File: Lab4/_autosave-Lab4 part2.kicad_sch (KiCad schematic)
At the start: 10 parts, among them J1 Conn_01x02_Male, U1 NE555D

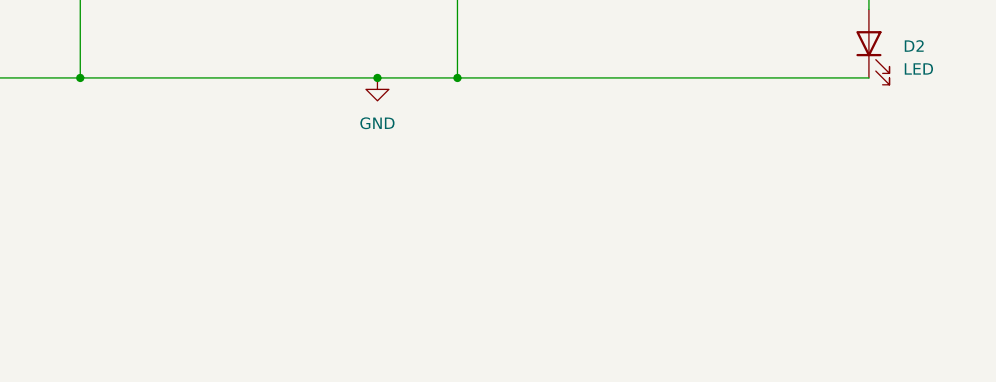
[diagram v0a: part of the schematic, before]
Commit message: Y direction and 2 netlabels update
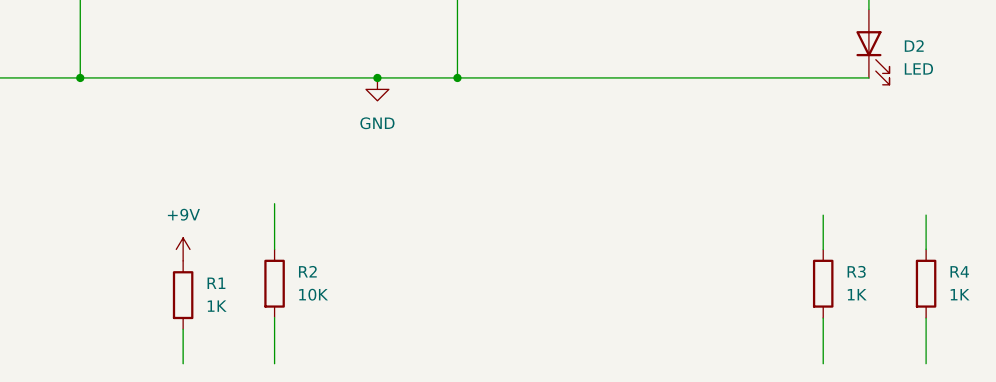
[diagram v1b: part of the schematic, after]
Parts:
- added R1, R3, R4: 1K, symbol Device:R
- added R2: 10K, symbol Device:R
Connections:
- net +9V: now also R1.1
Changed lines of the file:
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@@
+    (stroke (width 0) (type default) (color 0 0 0 0))
+  )
+  (wire (pts (xy 110.49 138.43) (xy 110.49 143.51))
+    (stroke (width 0) (type default) (color 0 0 0 0))
+  )
+  (wire (pts (xy 171.45 127) (xy 171.45 130.81))
     (stroke (width 0) (type default) (color 0 0 0 0))
   )
@@
     (stroke (width 0) (type default) (color 0 0 0 0))
   )
+  (wire (pts (xy 171.45 138.43) (xy 171.45 143.51))
+    (stroke (width 0) (type default) (color 0 0 0 0))
+  )
   (wire (pts (xy 69.85 87.63) (xy 69.85 97.79))
     (stroke (width 0) (type default) (color 0 0 0 0))
@@
     (stroke (width 0) (type default) (color 0 0 0 0))
   )
+  (wire (pts (xy 100.33 139.7) (xy 100.33 143.51))
+    (stroke (width 0) (type default) (color 0 0 0 0))
+  )
   (wire (pts (xy 60.96 68.58) (xy 69.85 68.58))
     (stroke (width 0) (type default) (color 0 0 0 0))
@@
     (stroke (width 0) (type default) (color 0 0 0 0))
   )
+  (wire (pts (xy 182.88 138.43) (xy 182.88 143.51))
+    (stroke (width 0) (type default) (color 0 0 0 0))
+  )
   (wire (pts (xy 110.49 81.28) (xy 118.11 81.28))
     (stroke (width 0) (type default) (color 0 0 0 0))
   )
+  (wire (pts (xy 182.88 127) (xy 182.88 130.81))
+    (stroke (width 0) (type default) (color 0 0 0 0))
+  )
   (wire (pts (xy 88.9 111.76) (xy 121.92 111.76))
     (stroke (width 0) (type default) (color 0 0 0 0))
@@
   )
   (wire (pts (xy 60.96 97.79) (xy 69.85 97.79))
+    (stroke (width 0) (type default) (color 0 0 0 0))
+  )
+  (wire (pts (xy 110.49 125.73) (xy 110.49 130.81))
     (stroke (width 0) (type default) (color 0 0 0 0))
   )
@@
     (effects (font (size 1.27 1.27)) (justify left bottom))
   )
+  (symbol (lib_id "Device:R") (at 171.45 134.62 0) (unit 1)
+    (in_bom yes) (on_board yes)
+    (property "Reference" "R3" (id 0) (at 173.99 133.3499 0)
+      (effects (font (size 1.27 1.27)) (justify left))
+    )
+    (property "Value" "1K" (id 1) (at 173.99 135.8899 0)
+      (effects (font (size 1.27 1.27)) (justify left))
+    )
+    (property "Footprint" "" (id 2) (at 169.672 134.62 90)
+      (effects (font (size 1.27 1.27)) hide)
+    )
+    (property "Datasheet" "~" (id 3) (at 171.45 134.62 0)
+      (effects (font (size 1.27 1.27)) hide)
+    )
+    (pin "1")
+    (pin "2")
+  )
   (symbol (lib_id "power:+9V") (at 124.46 25.4 0) (unit 1)
     (in_bom yes) (on_board yes) (fields_autoplaced)
-    (property "Reference" "#PWR?" (id 0) (at 124.46 29.21 0)
+    (property "Reference" "#PWR01" (id 0) (at 124.46 29.21 0)
       (effects (font (size 1.27 1.27)) hide)
     )
@@
     (pin "2")
   )
+  (symbol (lib_id "Device:R") (at 100.33 135.89 0) (unit 1)
+    (in_bom yes) (on_board yes) (fields_autoplaced)
+    (property "Reference" "R1" (id 0) (at 102.87 134.6199 0)
+      (effects (font (size 1.27 1.27)) (justify left))
+    )
+    (property "Value" "1K" (id 1) (at 102.87 137.1599 0)
+      (effects (font (size 1.27 1.27)) (justify left))
+    )
+    (property "Footprint" "" (id 2) (at 98.552 135.89 90)
+      (effects (font (size 1.27 1.27)) hide)
+    )
+    (property "Datasheet" "~" (id 3) (at 100.33 135.89 0)
+      (effects (font (size 1.27 1.27)) hide)
+    )
+    (pin "1")
+    (pin "2")
+  )
   (symbol (lib_id "Device:LED") (at 176.53 107.95 90) (unit 1)
     (in_bom yes) (on_board yes) (fields_autoplaced)
@@
   (symbol (lib_id "power:GND") (at 127 25.4 180) (unit 1)
     (in_bom yes) (on_board yes)
-    (property "Reference" "#PWR?" (id 0) (at 127 19.05 0)
+    (property "Reference" "#PWR02" (id 0) (at 127 19.05 0)
       (effects (font (size 1.27 1.27)) hide)
     )
@@
   (symbol (lib_id "power:+9V") (at 69.85 50.8 0) (unit 1)
     (in_bom yes) (on_board yes) (fields_autoplaced)
-    (property "Reference" "#PWR?" (id 0) (at 69.85 54.61 0)
+    (property "Reference" "#PWR04" (id 0) (at 69.85 54.61 0)
       (effects (font (size 1.27 1.27)) hide)
     )
@@
     (pin "2")
   )
+  (symbol (lib_id "Device:R") (at 182.88 134.62 0) (unit 1)
+    (in_bom yes) (on_board yes)
+    (property "Reference" "R4" (id 0) (at 185.42 133.3499 0)
+      (effects (font (size 1.27 1.27)) (justify left))
+    )
+    (property "Value" "1K" (id 1) (at 185.42 135.8899 0)
+      (effects (font (size 1.27 1.27)) (justify left))
+    )
+    (property "Footprint" "" (id 2) (at 181.102 134.62 90)
+      (effects (font (size 1.27 1.27)) hide)
+    )
+    (property "Datasheet" "~" (id 3) (at 182.88 134.62 0)
+      (effects (font (size 1.27 1.27)) hide)
+    )
+    (pin "1")
+    (pin "2")
+  )
   (symbol (lib_id "Device:R") (at 69.85 54.61 0) (unit 1)
     (in_bom yes) (on_board yes) (fields_autoplaced)
@@
   (symbol (lib_id "power:+9V") (at 176.53 44.45 0) (unit 1)
     (in_bom yes) (on_board yes) (fields_autoplaced)
-    (property "Reference" "#PWR?" (id 0) (at 176.53 48.26 0)
+    (property "Reference" "#PWR03" (id 0) (at 176.53 48.26 0)
       (effects (font (size 1.27 1.27)) hide)
     )
@@
     (pin "1")
   )
+  (symbol (lib_id "power:+9V") (at 100.33 132.08 0) (unit 1)
+    (in_bom yes) (on_board yes) (fields_autoplaced)
+    (property "Reference" "#PWR07" (id 0) (at 100.33 135.89 0)
+      (effects (font (size 1.27 1.27)) hide)
+    )
+    (property "Value" "+9V" (id 1) (at 100.33 127 0))
+    (property "Footprint" "" (id 2) (at 100.33 132.08 0)
+      (effects (font (size 1.27 1.27)) hide)
+    )
+    (property "Datasheet" "" (id 3) (at 100.33 132.08 0)
+      (effects (font (size 1.27 1.27)) hide)
+    )
+    (pin "1")
+  )
   (symbol (lib_id "power:GND") (at 121.92 111.76 0) (unit 1)
     (in_bom yes) (on_board yes) (fields_autoplaced)
-    (property "Reference" "#PWR?" (id 0) (at 121.92 118.11 0)
+    (property "Reference" "#PWR06" (id 0) (at 121.92 118.11 0)
       (effects (font (size 1.27 1.27)) hide)
     )
@@
   (symbol (lib_id "power:+9V") (at 130.81 58.42 0) (unit 1)
     (in_bom yes) (on_board yes) (fields_autoplaced)
-    (property "Reference" "#PWR?" (id 0) (at 130.81 62.23 0)
+    (property "Reference" "#PWR05" (id 0) (at 130.81 62.23 0)
       (effects (font (size 1.27 1.27)) hide)
     )
@@
     )
     (pin "1")
+  )
+  (symbol (lib_id "Device:R") (at 110.49 134.62 0) (unit 1)
+    (in_bom yes) (on_board yes) (fields_autoplaced)
+    (property "Reference" "R2" (id 0) (at 113.03 133.3499 0)
+      (effects (font (size 1.27 1.27)) (justify left))
+    )
+    (property "Value" "10K" (id 1) (at 113.03 135.8899 0)
+      (effects (font (size 1.27 1.27)) (justify left))
+    )
+    (property "Footprint" "" (id 2) (at 108.712 134.62 90)
+      (effects (font (size 1.27 1.27)) hide)
+    )
+    (property "Datasheet" "~" (id 3) (at 110.49 134.62 0)
+      (effects (font (size 1.27 1.27)) hide)
+    )
+    (pin "1")
+    (pin "2")
   )
   (symbol (lib_id "Device:R") (at 176.53 66.04 0) (unit 1)
@@
   (symbol_instances
     (path "/282a963d-bfb8-4d94-9bf6-62b851b06003"
-      (reference "#PWR?") (unit 1) (value "+9V") (footprint "")
+      (reference "#PWR01") (unit 1) (value "+9V") (footprint "")
     )
     (path "/5d09f4c4-a044-47ca-ac71-306d51ef7f90"
-      (reference "#PWR?") (unit 1) (value "GND") (footprint "")
+      (reference "#PWR02") (unit 1) (value "GND") (footprint "")
+    )
+    (path "/b412588f-978c-4331-ae0a-8423d483384c"
+      (reference "#PWR03") (unit 1) (value "+9V") (footprint "")
     )
     (path "/74069aab-7706-4166-a931-cdf4c5448779"
-      (reference "#PWR?") (unit 1) (value "+9V") (footprint "")
-    )
-    (path "/b412588f-978c-4331-ae0a-8423d483384c"
-      (reference "#PWR?") (unit 1) (value "+9V") (footprint "")
+      (reference "#PWR04") (unit 1) (value "+9V") (footprint "")
+    )
+    (path "/c17c992d-526c-4279-bbbc-3fdfc491b0ff"
+      (reference "#PWR05") (unit 1) (value "+9V") (footprint "")
     )
     (path "/bcee0015-7b8e-4b42-a656-2b391cf11282"
-      (reference "#PWR?") (unit 1) (value "GND") (footprint "")
-    )
-    (path "/c17c992d-526c-4279-bbbc-3fdfc491b0ff"
-      (reference "#PWR?") (unit 1) (value "+9V") (footprint "")
+      (reference "#PWR06") (unit 1) (value "GND") (footprint "")
+    )
+    (path "/b8ebe7e4-57a8-4fda-9b97-02cec9d370ef"
+      (reference "#PWR07") (unit 1) (value "+9V") (footprint "")
     )
     (path "/c045f09e-98f2-4d47-a454-cfd2caa9b0cd"
@@
       (reference "J1") (unit 1) (value "Conn_01x02_Male") (footprint "")
     )
+    (path "/4cc59900-8c63-40da-899a-0fa5b085c4e7"
+      (reference "R1") (unit 1) (value "1K") (footprint "")
+    )
     (path "/b3516c82-4832-4970-a96f-5101ef3a446b"
       (reference "R1") (unit 1) (value "1K") (footprint "")
     )
+    (path "/cf21566b-861a-4450-a59b-8a46c6eb49e6"
+      (reference "R2") (unit 1) (value "10K") (footprint "")
+    )
     (path "/f7a918f5-f477-4015-8f3d-6de4b24bd234"
       (reference "R2") (unit 1) (value "10K") (footprint "")
     )
+    (path "/26e5687a-a9a4-4ea7-a907-b7227bd379be"
+      (reference "R3") (unit 1) (value "1K") (footprint "")
+    )
     (path "/cf7958ac-92d6-425c-a5fd-922d040e6583"
       (reference "R3") (unit 1) (value "1K") (footprint "")
@@
       (reference "R4") (unit 1) (value "1K") (footprint "")
     )
+    (path "/a8646c1a-54d9-48fa-b726-fc95525641af"
+      (reference "R4") (unit 1) (value "1K") (footprint "")
+    )

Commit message: latest update part2
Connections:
- net pin_2: now also C1.1, R2.2, R2.2
- net pin_3: now also R3.2, R3.2, R4.1
- net pin_7: now also R1.2, R2.1
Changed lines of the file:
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@@
+    (stroke (width 0) (type default) (color 0 0 0 0))
+  )
+  (wire (pts (xy 110.49 143.51) (xy 118.11 143.51))
     (stroke (width 0) (type default) (color 0 0 0 0))
   )
@@
     (stroke (width 0) (type default) (color 0 0 0 0))
   )
+  (wire (pts (xy 100.33 139.7) (xy 100.33 142.24))
+    (stroke (width 0) (type default) (color 0 0 0 0))
+  )
+  (wire (pts (xy 110.49 125.73) (xy 118.11 125.73))
+    (stroke (width 0) (type default) (color 0 0 0 0))
+  )
   (wire (pts (xy 69.85 58.42) (xy 69.85 68.58))
+    (stroke (width 0) (type default) (color 0 0 0 0))
+  )
+  (wire (pts (xy 171.45 143.51) (xy 177.8 143.51))
     (stroke (width 0) (type default) (color 0 0 0 0))
   )
@@
   )
   (wire (pts (xy 88.9 93.98) (xy 88.9 76.2))
-    (stroke (width 0) (type default) (color 0 0 0 0))
-  )
-  (wire (pts (xy 100.33 139.7) (xy 100.33 143.51))
     (stroke (width 0) (type default) (color 0 0 0 0))
   )
@@
     (stroke (width 0) (type default) (color 0 0 0 0))
   )
+  (wire (pts (xy 92.71 142.24) (xy 100.33 142.24))
+    (stroke (width 0) (type default) (color 0 0 0 0))
+  )
   (wire (pts (xy 69.85 97.79) (xy 69.85 104.14))
     (stroke (width 0) (type default) (color 0 0 0 0))
@@
     (effects (font (size 1.27 1.27)) (justify left bottom))
   )
+  (label "pin_2" (at 60.96 97.79 0)
+    (effects (font (size 1.27 1.27)) (justify left bottom))
+  )
   (label "pin_7" (at 148.59 76.2 0)
+    (effects (font (size 1.27 1.27)) (justify left bottom))
+  )
+  (label "pin_3" (at 180.34 76.2 0)
+    (effects (font (size 1.27 1.27)) (justify left bottom))
+  )
+  (label "pin_7" (at 113.03 125.73 0)
+    (effects (font (size 1.27 1.27)) (justify left bottom))
+  )
+  (label "pin_2" (at 113.03 143.51 0)
     (effects (font (size 1.27 1.27)) (justify left bottom))
   )
@@
     (effects (font (size 1.27 1.27)) (justify left bottom))
   )
+  (label "pin_7" (at 92.71 142.24 0)
+    (effects (font (size 1.27 1.27)) (justify left bottom))
+  )
   (label "pin_3" (at 148.59 71.12 0)
     (effects (font (size 1.27 1.27)) (justify left bottom))
   )
+  (label "pin_3" (at 172.72 143.51 0)
+    (effects (font (size 1.27 1.27)) (justify left bottom))
+  )
